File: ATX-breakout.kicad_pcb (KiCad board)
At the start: 2 copper layers, 67 x 59.5 mm, 27 parts, among them J1 I2C, J10 3V3 out, J11 12V out, J12 12V out, J2 EPS, J3 USB_A, J4 Raspberry_Pi_2_3, J5 ATX24pin, J6 12V out, J7 pson ext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

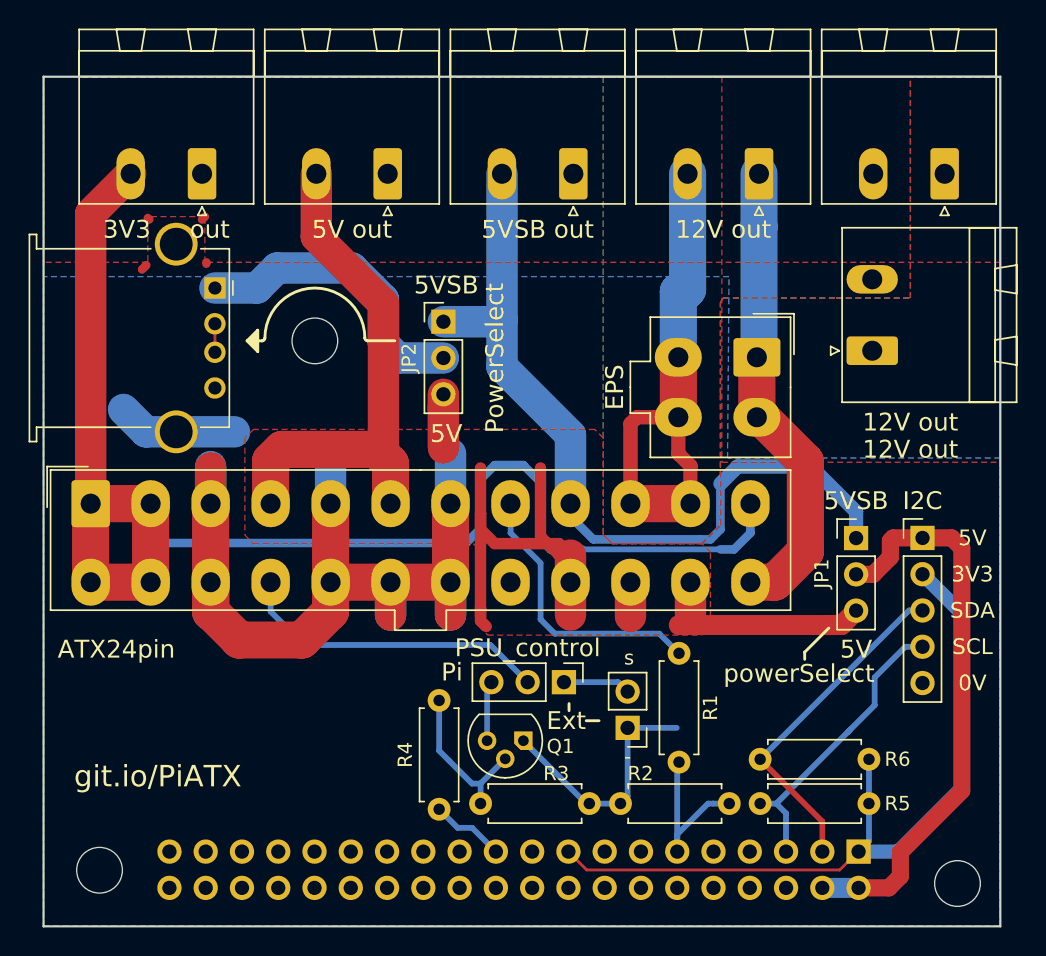
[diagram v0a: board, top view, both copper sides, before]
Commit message: Updated silkscreen
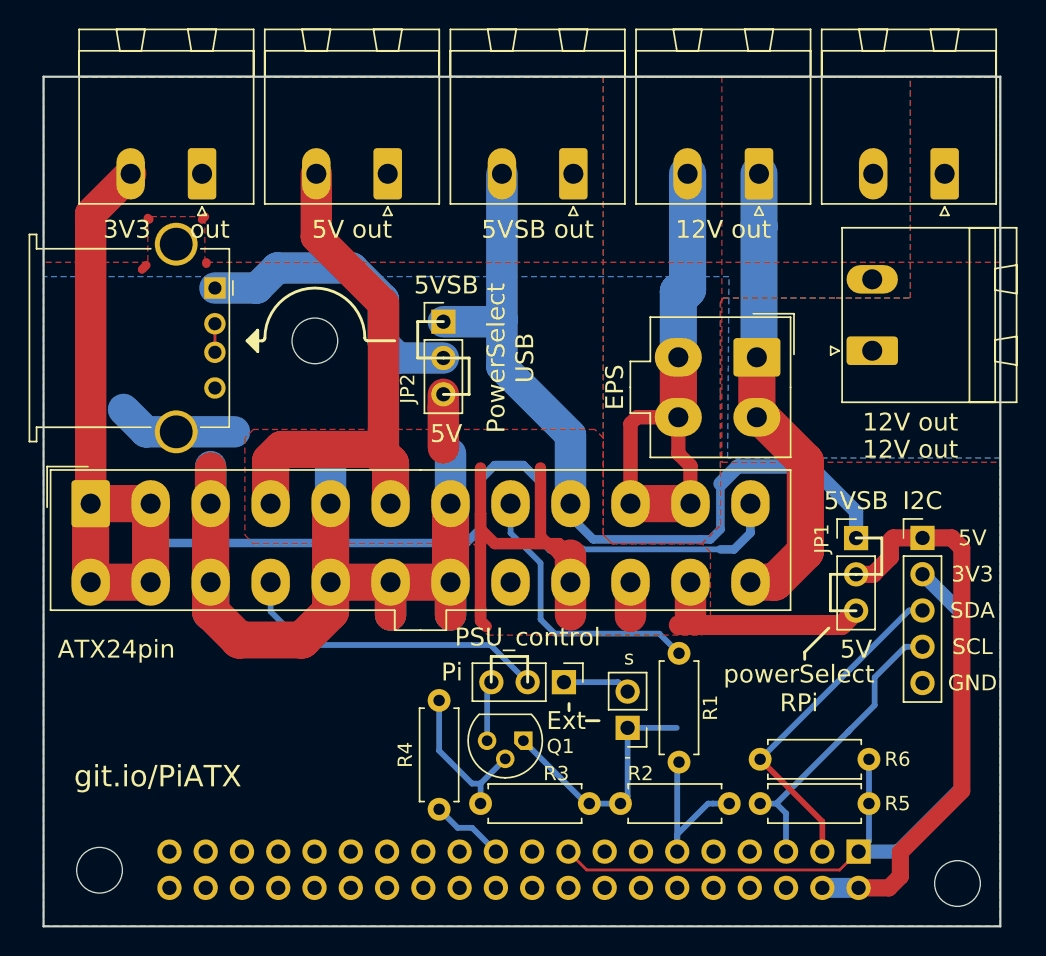
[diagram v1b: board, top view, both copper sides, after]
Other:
- board text added: "GND"
- board text added: "PowerSelect USB"
- board text added: "powerSelect RPi"
- board text removed: "0V"
- board text removed: "PowerSelect"
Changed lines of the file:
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@@
-(kicad_pcb (version 20171130) (host pcbnew "(5.0.1-dev-70-gb7b125d83)")
+(kicad_pcb (version 20171130) (host pcbnew 5.0.2-5.fc29)
   (general
     (thickness 1.6)
-    (drawings 61)
+    (drawings 77)
     (tracks 208)
     (zones 0)
@@
     (descr "Through hole straight pin header, 1x03, 2.54mm pitch, single row")
     (tags "Through hole pin header THT 1x03 2.54mm single row")
-    (fp_text reference JP1 (at -2.4 2.49 90) (layer F.SilkS)
-      (effects (font (size 1 1) (thickness 0.15)))
-    )
-    (fp_text value powerSelect (at -4 9.49 180) (layer F.SilkS)
+    (fp_text reference JP1 (at -2.4 0.04 270) (layer F.SilkS)
+      (effects (font (size 1 1) (thickness 0.15)))
+    )
+    (fp_text value powerSelect (at -4 9.49 180) (layer F.SilkS) hide
       (effects (font (size 1.25 1.25) (thickness 0.2)))
     )
@@
     (descr "Through hole straight pin header, 1x03, 2.54mm pitch, single row")
     (tags "Through hole pin header THT 1x03 2.54mm single row")
-    (fp_text reference JP2 (at -2.4 2.54 90) (layer F.SilkS)
+    (fp_text reference JP2 (at -2.5 4.69 90) (layer F.SilkS)
       (effects (font (size 1 1) (thickness 0.15)))
     )
@@
       (effects (font (size 1 1) (thickness 0.15)))
     )
-    (fp_text value PSU_control (at -2.4 2.54 180) (layer F.SilkS)
+    (fp_text value PSU_control (at -3.15 2.54 180) (layer F.SilkS)
       (effects (font (size 1.25 1.25) (thickness 0.2)))
     )
@@
     (pad 1 np_thru_hole circle (at 0 0) (size 3.2 3.2) (drill 3.2) (layers *.Cu *.Mask))
   )
+  (gr_line (start 29.8 22.25) (end 28 22.25) (layer F.SilkS) (width 0.2))
+  (gr_line (start 28 19.7) (end 29.8 19.7) (layer F.SilkS) (width 0.2))
+  (gr_line (start 29.8 19.7) (end 29.8 22.25) (layer F.SilkS) (width 0.2))
+  (gr_line (start 28 19.7) (end 26.2 19.7) (layer F.SilkS) (width 0.2))
+  (gr_line (start 26.2 17.15) (end 28 17.15) (layer F.SilkS) (width 0.2))
+  (gr_line (start 26.2 19.7) (end 26.2 17.15) (layer F.SilkS) (width 0.2))
+  (gr_line (start 56.9 37.4) (end 55.1 37.4) (layer F.SilkS) (width 0.2))
+  (gr_line (start 55.1 34.85) (end 56.9 34.85) (layer F.SilkS) (width 0.2))
+  (gr_line (start 55.1 37.4) (end 55.1 34.85) (layer F.SilkS) (width 0.2))
+  (gr_line (start 58.7 34.85) (end 56.9 34.85) (layer F.SilkS) (width 0.2))
+  (gr_line (start 56.9 32.3) (end 58.7 32.3) (layer F.SilkS) (width 0.2))
+  (gr_line (start 58.7 32.3) (end 58.7 34.85) (layer F.SilkS) (width 0.2))
+  (gr_line (start 33.9 40.6) (end 33.9 42.4) (layer F.SilkS) (width 0.2))
+  (gr_line (start 31.35 40.6) (end 33.9 40.6) (layer F.SilkS) (width 0.2))
+  (gr_line (start 31.35 42.4) (end 31.35 40.6) (layer F.SilkS) (width 0.2))
+  (gr_text "powerSelect\nRPi" (at 52.9 42.85) (layer F.SilkS)
+    (effects (font (size 1.25 1.25) (thickness 0.2)))
+  )
   (gr_line (start 1.2 2.8) (end 1.4 2.6) (layer B.SilkS) (width 0.2))
   (gr_text y (at 1.4 3.6 270) (layer B.SilkS)
@@
     (effects (font (size 1 1) (thickness 0.15)) (justify mirror))
   )
-  (gr_text 0V (at 65.048 42.46) (layer F.SilkS)
+  (gr_text GND (at 65.048 42.46) (layer F.SilkS)
     (effects (font (size 1.1 1.1) (thickness 0.18)))
   )
@@
     (effects (font (size 1.25 1.25) (thickness 0.2)))
   )
-  (gr_text PowerSelect (at 31.6 19.7 90) (layer F.SilkS)
+  (gr_text "PowerSelect\nUSB" (at 32.7 19.7 90) (layer F.SilkS)
     (effects (font (size 1.25 1.25) (thickness 0.2)))
   )
